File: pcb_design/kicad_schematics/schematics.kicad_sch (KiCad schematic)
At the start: 16 parts, among them J1 Conn_01x02_Pin, J2 Conn_01x01_Pin, J3 SG90_01x03_Pin, J4 Conn_01x01_Pin, J5 Conn_01x01_Pin, U1 PIC24FJ64GA702-I_SO, U2 ESP8266-01_ESP-01

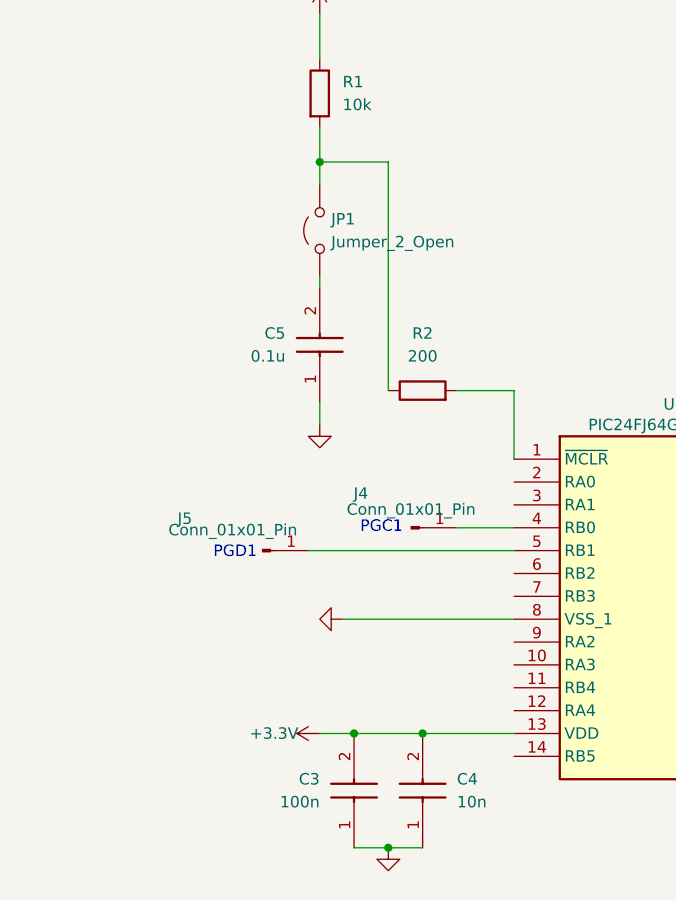
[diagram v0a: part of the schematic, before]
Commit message: ICSP pinovi
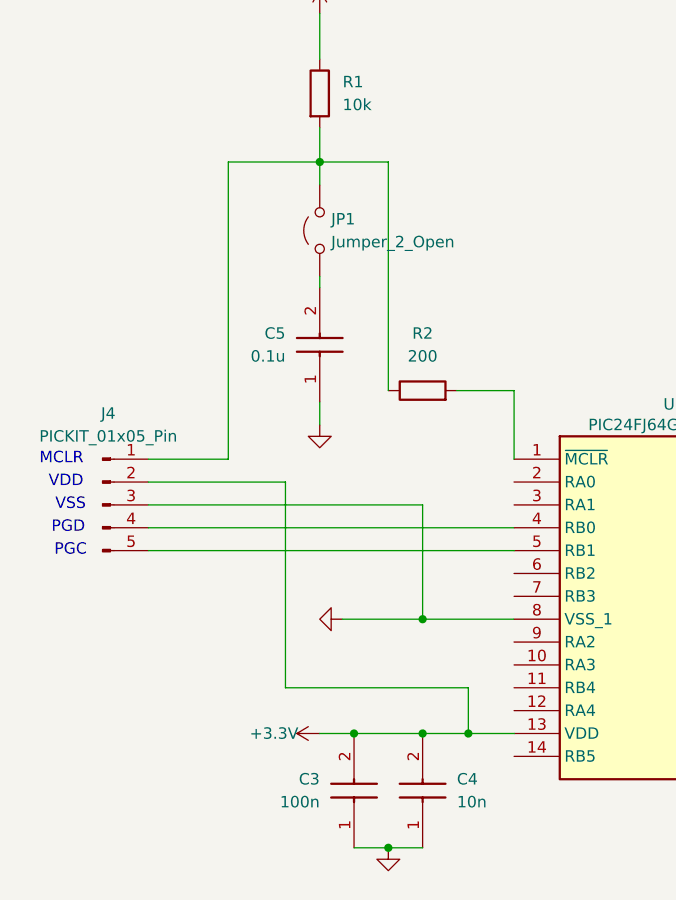
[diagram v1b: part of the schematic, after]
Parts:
- removed J4, J5: Conn_01x01_Pin, symbol Connector:Conn_01x01_Pin
- added J4: PICKIT_01x05_Pin, symbol Connector:Conn_01x05_Pin
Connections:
- net +3.3V: now also J4.2 (Pin_2)
- net GND: now also J4.3 (Pin_3)
- net at U1.4 (RB0): now also J4.4 (Pin_4)
- net at U1.5 (RB1): now also J4.5 (Pin_5)
- net at JP1.2 (B), R1.2, R2.1: now also J4.1 (Pin_1)
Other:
- note added: "MCLR"
- note added: "PGC"
- note added: "PGD"
- note added: "VDD"
- note added: "VSS"
- note removed: "PGC1"
- note removed: "PGD1"
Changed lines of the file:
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@@
+	)
+	(junction
+		(at 71.12 104.14)
+		(diameter 0)
+		(color 0 0 0 0)
 	)
 	(junction
@@
 	)
 	(junction
+		(at 66.04 91.44)
+		(diameter 0)
+		(color 0 0 0 0)
+	)
+	(junction
 		(at 121.92 58.42)
 		(diameter 0)
@@
 	(wire
 		(pts
+			(xy 50.8 76.2) (xy 50.8 99.06)
+		)
+		(stroke
+			(width 0)
+			(type default)
+		)
+	)
+	(wire
+		(pts
 			(xy 121.92 58.42) (xy 121.92 73.66)
 		)
@@
 	(wire
 		(pts
+			(xy 35.56 78.74) (xy 66.04 78.74)
+		)
+		(stroke
+			(width 0)
+			(type default)
+		)
+	)
+	(wire
+		(pts
 			(xy 190.5 83.82) (xy 190.5 99.06)
 		)
@@
 	(wire
 		(pts
-			(xy 66.04 104.14) (xy 76.2 104.14)
+			(xy 66.04 104.14) (xy 71.12 104.14)
 		)
 		(stroke
@@
 	(wire
 		(pts
+			(xy 35.56 76.2) (xy 50.8 76.2)
+		)
+		(stroke
+			(width 0)
+			(type default)
+		)
+	)
+	(wire
+		(pts
 			(xy 121.92 57.15) (xy 121.92 58.42)
 		)
@@
 	(wire
 		(pts
+			(xy 71.12 99.06) (xy 71.12 104.14)
+		)
+		(stroke
+			(width 0)
+			(type default)
+		)
+	)
+	(wire
+		(pts
 			(xy 243.84 88.9) (xy 238.76 88.9)
 		)
@@
 	(wire
 		(pts
+			(xy 66.04 78.74) (xy 66.04 91.44)
+		)
+		(stroke
+			(width 0)
+			(type default)
+		)
+	)
+	(wire
+		(pts
 			(xy 134.62 96.52) (xy 134.62 102.87)
 		)
@@
 	(wire
 		(pts
+			(xy 44.45 73.66) (xy 44.45 40.64)
+		)
+		(stroke
+			(width 0)
+			(type default)
+		)
+	)
+	(wire
+		(pts
 			(xy 195.58 93.98) (xy 203.2 93.98)
 		)
@@
 	(wire
 		(pts
+			(xy 44.45 40.64) (xy 54.61 40.64)
+		)
+		(stroke
+			(width 0)
+			(type default)
+		)
+	)
+	(wire
+		(pts
 			(xy 127 144.78) (xy 127 101.6)
 		)
@@
 	(wire
 		(pts
-			(xy 57.15 91.44) (xy 76.2 91.44)
+			(xy 35.56 83.82) (xy 76.2 83.82)
+		)
+		(stroke
+			(width 0)
+			(type default)
+		)
+	)
+	(wire
+		(pts
+			(xy 35.56 81.28) (xy 76.2 81.28)
+		)
+		(stroke
+			(width 0)
+			(type default)
+		)
+	)
+	(wire
+		(pts
+			(xy 57.15 91.44) (xy 66.04 91.44)
 		)
 		(stroke
@@
 	(wire
 		(pts
-			(xy 69.85 81.28) (xy 76.2 81.28)
-		)
-		(stroke
-			(width 0)
-			(type default)
-		)
-	)
-	(wire
-		(pts
 			(xy 252.73 104.14) (xy 238.76 104.14)
 		)
@@
 	(wire
 		(pts
+			(xy 66.04 91.44) (xy 76.2 91.44)
+		)
+		(stroke
+			(width 0)
+			(type default)
+		)
+	)
+	(wire
+		(pts
 			(xy 121.92 73.66) (xy 111.76 73.66)
 		)
@@
 	(wire
 		(pts
+			(xy 35.56 73.66) (xy 44.45 73.66)
+		)
+		(stroke
+			(width 0)
+			(type default)
+		)
+	)
+	(wire
+		(pts
+			(xy 71.12 104.14) (xy 76.2 104.14)
+		)
+		(stroke
+			(width 0)
+			(type default)
+		)
+	)
+	(wire
+		(pts
 			(xy 189.23 101.6) (xy 203.2 101.6)
 		)
@@
 	(wire
 		(pts
-			(xy 53.34 83.82) (xy 76.2 83.82)
+			(xy 50.8 99.06) (xy 71.12 99.06)
 		)
 		(stroke
@@
 			(width 0)
 			(type default)
+		)
+	)
+	(text "VDD"
+		(exclude_from_sim no)
+		(at 26.416 76.2 0)
+		(effects
+			(font
+				(size 1.27 1.27)
+				(color 0 0 0 1)
+			)
 		)
 	)
@@
 		)
 	)
-	(text "PGC1"
-		(exclude_from_sim no)
-		(at 61.468 81.28 0)
+	(text "PGC"
+		(exclude_from_sim no)
+		(at 26.924 83.82 0)
 		(effects
 			(font
@@
 		)
 	)
-	(text "PGD1"
-		(exclude_from_sim no)
-		(at 45.212 84.074 0)
+	(text "VSS"
+		(exclude_from_sim no)
+		(at 26.924 78.74 0)
+		(effects
+			(font
+				(size 1.27 1.27)
+				(color 0 0 0 1)
+			)
+		)
+	)
+	(text "MCLR"
+		(exclude_from_sim no)
+		(at 25.908 73.66 0)
+		(effects
+			(font
+				(size 1.27 1.27)
+				(color 0 0 0 1)
+			)
+		)
+	)
+	(text "PGD"
+		(exclude_from_sim no)
+		(at 26.67 81.28 0)
 		(effects
 			(font
@@
 	)
 	(symbol
+		(lib_id "Connector:Conn_01x05_Pin")
+		(at 30.48 78.74 0)
+		(unit 1)
+		(exclude_from_sim no)
+		(in_bom yes)
+		(on_board yes)
+		(dnp no)
+		(fields_autoplaced yes)
+		(property "Reference" "J4"
+			(at 31.115 68.58 0)
+			(effects
+				(font
+					(size 1.27 1.27)
+				)
+			)
+		)
+		(property "Value" "PICKIT_01x05_Pin"
+			(at 31.115 71.12 0)
+			(effects
+				(font
+					(size 1.27 1.27)
+				)
+			)
+		)
+		(property "Footprint" ""
+			(at 30.48 78.74 0)
+			(effects
+				(font
+					(size 1.27 1.27)
+				)
+				(hide yes)
+			)
+		)
+		(property "Datasheet" "~"
+			(at 30.48 78.74 0)
+			(effects
+				(font
+					(size 1.27 1.27)
+				)
+				(hide yes)
+			)
+		)
+		(property "Description" "Generic connector, single row, 01x05, script generated"
+			(at 30.48 78.74 0)
+			(effects
+				(font
+					(size 1.27 1.27)
+				)
+				(hide yes)
+			)
+		)
+		(pin "1"
+		)
+		(pin "3"
+		)
+		(pin "2"
+		)
+		(pin "4"
+		)
+		(pin "5"
+		)
+		(instances
+			(project ""
+				(path "/be652b9a-b406-4c1b-9f3b-1d87964716dc"
+					(reference "J4")
+					(unit 1)
+				)
+			)
+		)
+	)
+	(symbol
 		(lib_id "power:GND")
 		(at 143.51 102.87 90)
@@
 				(path "/be652b9a-b406-4c1b-9f3b-1d87964716dc"
 					(reference "#PWR07")
-					(unit 1)
-				)
-			)
-		)
-	)
-	(symbol
-		(lib_name "Conn_01x01_Pin_2")
-		(lib_id "Connector:Conn_01x01_Pin")
-		(at 64.77 81.28 0)
-		(unit 1)
-		(exclude_from_sim no)
-		(in_bom yes)
-		(on_board yes)
-		(dnp no)
-		(property "Reference" "J4"
-			(at 59.182 77.47 0)
-			(effects
-				(font
-					(size 1.27 1.27)
-				)
-			)
-		)
-		(property "Value" "Conn_01x01_Pin"
-			(at 64.77 79.248 0)
-			(effects
-				(font
-					(size 1.27 1.27)
-				)
-			)
-		)
-		(property "Footprint" ""
-			(at 64.77 81.28 0)
-			(effects
-				(font
-					(size 1.27 1.27)
-				)
-				(hide yes)
-			)
-		)
-		(property "Datasheet" "~"
-			(at 64.77 81.28 0)
-			(effects
-				(font
-					(size 1.27 1.27)
-				)
-				(hide yes)
-			)
-		)
-		(property "Description" "Generic connector, single row, 01x01, script generated"
-			(at 64.77 81.28 0)
-			(effects
-				(font
-					(size 1.27 1.27)
-				)
-				(hide yes)
-			)
-		)
-		(pin "1"
-		)
-		(instances
-			(project ""
-				(path "/be652b9a-b406-4c1b-9f3b-1d87964716dc"
-					(reference "J4")
 					(unit 1)
 				)
@@
 					(unit 1)
 				)
-			)
-		)
-	)
-	(symbol
-		(lib_name "Conn_01x01_Pin_1")
-		(lib_id "Connector:Conn_01x01_Pin")
-		(at 48.26 83.82 0)
-		(unit 1)
-		(exclude_from_sim no)
-		(in_bom yes)
-		(on_board yes)
-		(dnp no)
-		(property "Reference" "J5"
-			(at 39.624 80.264 0)
-			(effects
-				(font
-					(size 1.27 1.27)
-				)
-			)
-		)
-		(property "Value" "Conn_01x01_Pin"
-			(at 44.958 81.534 0)
-			(effects
-				(font
-					(size 1.27 1.27)
-				)
-			)
-		)
-		(property "Footprint" ""
-			(at 48.26 83.82 0)
-			(effects
-				(font
-					(size 1.27 1.27)
-				)
-				(hide yes)
-			)
-		)
-		(property "Datasheet" "~"
-			(at 48.26 83.82 0)
-			(effects
-				(font
-					(size 1.27 1.27)
-				)
-				(hide yes)
-			)
-		)
-		(property "Description" "Generic connector, single row, 01x01, script generated"
-			(at 48.26 83.82 0)
-			(effects
-				(font
-					(size 1.27 1.27)
-				)
-				(hide yes)
-			)
-		)
-		(pin "1"
-		)
-		(instances
-			(project ""
-				(path "/be652b9a-b406-4c1b-9f3b-1d87964716dc"
-					(reference "J5")
-					(unit 1)
-				)

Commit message: sema
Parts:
- removed J1: Conn_01x02_Pin, symbol Connector:Conn_01x02_Pin
- removed J2: Conn_01x01_Pin, symbol Connector:Conn_01x01_Pin
- added C7, C8: 10u, T495B106K025ATE750:CAPPC3528X210N, symbol T495B106K025ATE750:T495B106K025ATE750
- added J1: Conn_01x05_Pin, symbol Connector:Conn_01x05_Pin
- added J2: LED-HSF08A/B, symbol Connector:Conn_01x03_Pin
- added J5: BUTTON-HS-KEY1B, symbol Connector:Conn_01x03_Pin
- added U3: LM1117LD-3.3, Package_SON:WSON-8-1EP_4x4mm_P0.8mm_EP2.2x3mm, symbol Regulator_Linear:LM1117LD-3.3
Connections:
- net +3.3V: now also J1.1 (Pin_1), J2.2 (Pin_2), J5.2 (Pin_2)
- net GND: now also C7.2, C8.2, J1.5 (Pin_5), J2.3 (Pin_3), J5.3 (Pin_3), U3.1 (GND)
- net I2C_SCL_1: now also J1.3 (Pin_3)
- net I2C_SDA_1: now also J1.2 (Pin_2)
- net OCM1A: now also J1.4 (Pin_4)
- net at U1.11 (RB4): now also J2.1 (Pin_1)
- net at U1.12 (RA4): now also J5.1 (Pin_1)
- net +5V renamed +4.5V
- new net 3.3V: C8.1, U3.5 (VO), U3.6 (VO), U3.7 (VO), U3.9 (VO)
- new net Vin: C7.1, U3.2 (VI), U3.3 (VI), U3.4 (VI)
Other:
- moved on the sheet: C1, C2, C3, C4, C5, C6, J3, J4, JP1, R1, R2, U1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

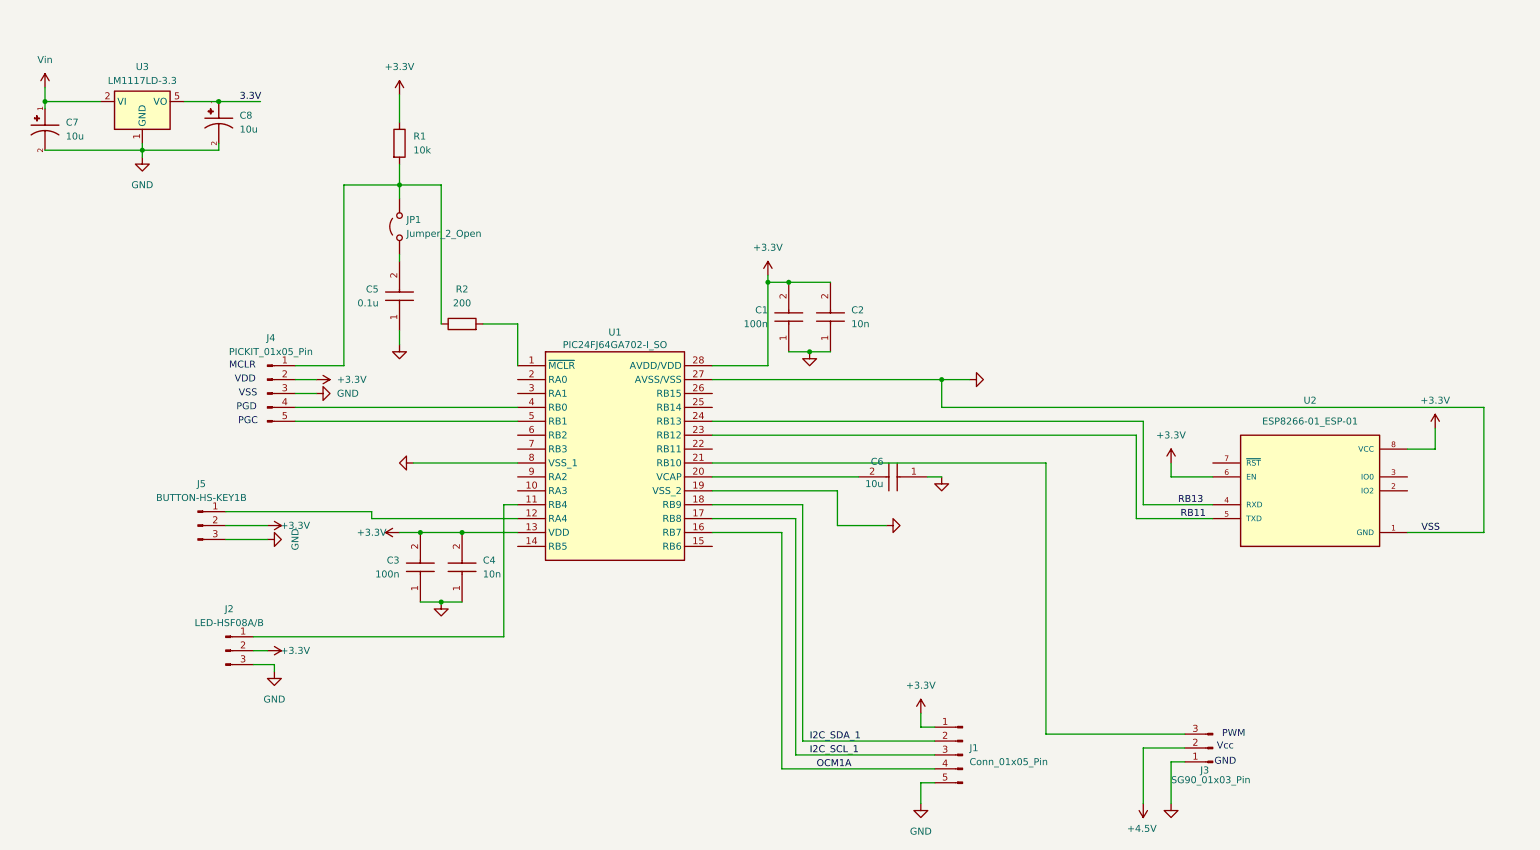
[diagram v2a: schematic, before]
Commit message: #11 Analiza power supply šeme Dodan je lin. regulator u semi
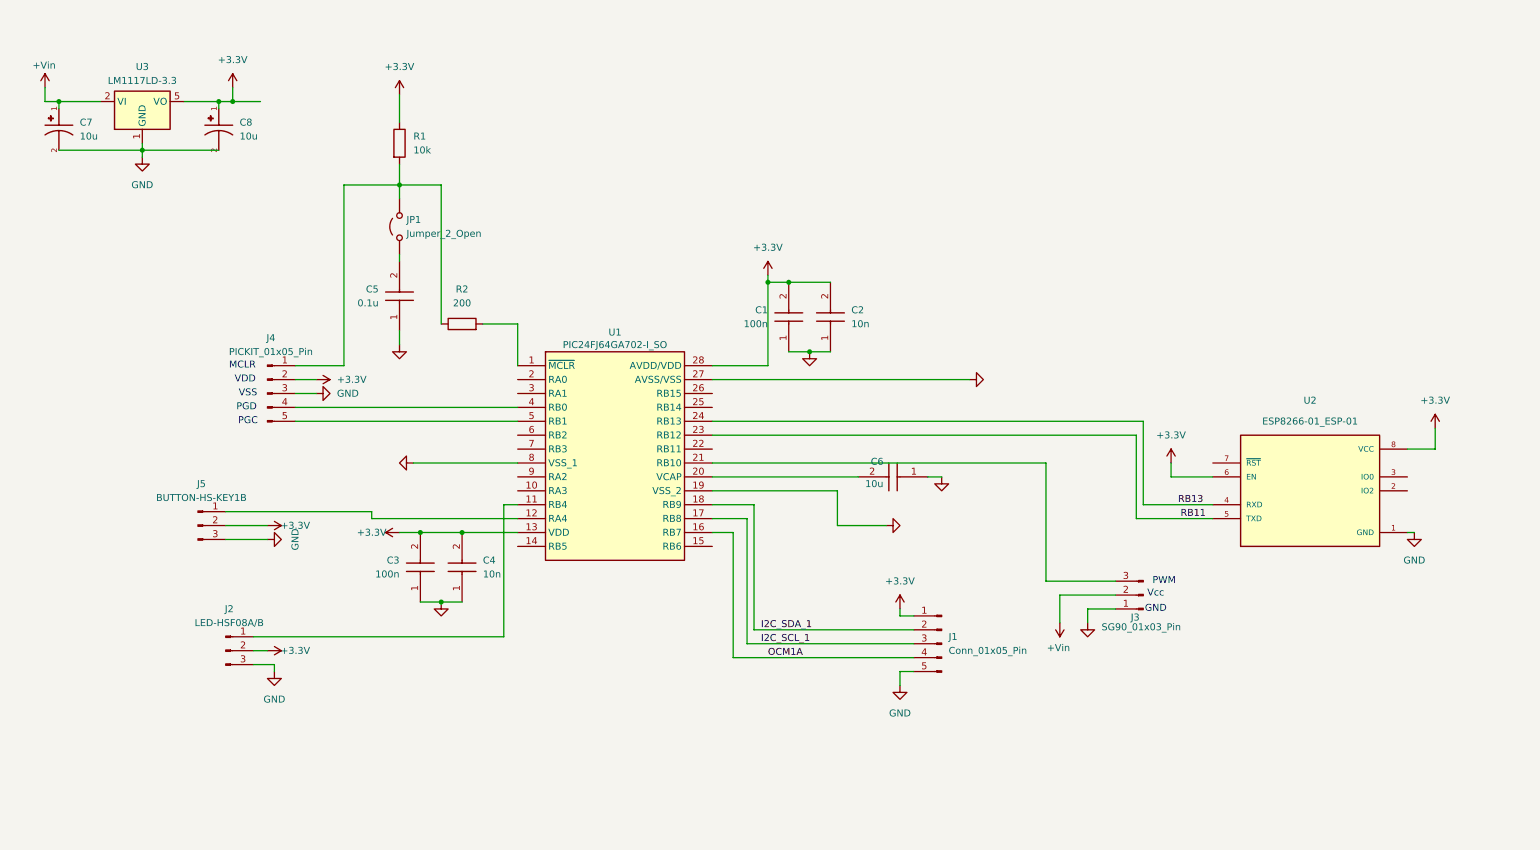
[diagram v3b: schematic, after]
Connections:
- net 3.3V is gone; now on net +3.3V: C8.1, U3.5 (VO), U3.6 (VO), U3.7 (VO), U3.9 (VO)
- net Vin is gone; now on net +Vin: C7.1, U3.2 (VI), U3.3 (VI), U3.4 (VI)
- net +4.5V renamed +Vin
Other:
- moved on the sheet: C7, C8, J1, J3

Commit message: Dodajem modele X5R capacitors koji su korišćeni u šemi
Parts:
- removed C1, C3: 100n, C0805, symbol C0805C106M4PACTU:C0805C106M4PACTU
- added C1, C3: 100u, CAPC2012X145N, symbol CL21X107MRYN3WE:CL21X107MRYN3WE
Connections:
- net +3.3V: now also C1.2, C3.2
- net GND: now also C1.1, C3.1

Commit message: Komentari sastanka
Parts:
- C1, C3: value 100u -> 100n
- C2, C4: value 10n -> 10u
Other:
- note added: "Dodati decoupling capacitors"
- note added: "Dodati jos jedan decoupling capacitor 10n"
- note added: "Konfigurasti external oscillator"
- note added: "Naci na internetu otpornike"
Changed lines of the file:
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@@
 		)
 	)
+	(text "Naci na internetu otpornike"
+		(exclude_from_sim no)
+		(at 104.394 60.96 0)
+		(effects
+			(font
+				(size 1.27 1.27)
+			)
+		)
+	)
 	(text "PWM"
 		(exclude_from_sim no)
@@
 		)
 	)
+	(text "Dodati decoupling capacitors"
+		(exclude_from_sim no)
+		(at 248.412 81.026 0)
+		(effects
+			(font
+				(size 1.27 1.27)
+			)
+		)
+	)
 	(text "VSS"
 		(exclude_from_sim no)
@@
 		)
 	)
+	(text "Dodati jos jedan decoupling capacitor 10n\n"
+		(exclude_from_sim no)
+		(at 43.434 18.288 0)
+		(effects
+			(font
+				(size 1.27 1.27)
+			)
+		)
+	)
+	(text "Konfigurasti external oscillator"
+		(exclude_from_sim no)
+		(at 84.074 91.44 0)
+		(effects
+			(font
+				(size 1.27 1.27)
+			)
+		)
+	)
 	(label "RB13"
 		(at 224.79 102.87 0)
@@
 			)
 		)
-		(property "Value" "100u"
+		(property "Value" "100n"
 			(at 149.86 69.8499 90)
 			(effects
@@
 			)
 		)
-		(property "Value" "100u"
+		(property "Value" "100n"
 			(at 82.55 115.5699 90)
 			(effects
@@
 			)
 		)
-		(property "Value" "10n"
+		(property "Value" "10u"
 			(at 97.79 115.5699 90)
 			(effects
@@
 			)
 		)
-		(property "Value" "10n"
+		(property "Value" "10u"
 			(at 165.1 69.8499 90)
 			(effects
